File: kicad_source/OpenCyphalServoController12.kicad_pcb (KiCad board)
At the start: 2 copper layers, 81 x 57 mm, 90 parts, among them CN1 SM04B-SRSS-TB, CN10 GH_SM04B-GHS-TB, CN11 GH_SM04B-GHS-TB, CN12 Powerpole_2, CN13 DNI, CN14 DNI, CN2 CONN_02X03, CN3 CONN_02X03, CN4 CONN_02X03, CN5 CONN_02X03, CN6 CONN_02X03, CN7 CONN_02X03, CN8 SM04B-SRSS-TB, CN9 RASPBERRYPI_PICO, SW1 SPST, U1 24LC64, U2 MCP2515, U3 SN65HVD232, U4 RAA211650, Y1 16MHz

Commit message: started layout
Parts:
- moved L1 111.5 mm to (117.1, 68.4)
- moved L2 108.7 mm to (121.1, 80.4)
- moved L3 58.4 mm to (87.0, 92.0)
- moved C17 8.96 mm to (90.0, 73.1), turned to -90 degrees
- moved R18 8.06 mm to (94.0, 96.0)
- moved C3 8.00 mm to (94.0, 97.6)
- moved R17 8.00 mm to (94.0, 100.2)
- moved C12 5.54 mm to (92.4, 69.2), turned to 180 degrees
- moved R16 4.12 mm to (102.0, 96.0)
- moved R21 4.12 mm to (98.0, 96.0)
- moved C2 4.00 mm to (102.0, 97.6)
- moved C4 4.00 mm to (98.0, 97.6)
- moved R15 4.00 mm to (102.0, 100.2)
- moved R20 4.00 mm to (98.0, 100.2)
- moved R11 2.00 mm to (110.0, 62.0)
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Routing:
- net GND: track 0.00 -> 200.6 mm, vias 0 -> 23
- net VCC: track 0.00 -> 200.5 mm, vias 0 -> 4
- net +3V3: track 0.23 -> 162.8 mm, vias 0 -> 6
- net +BATT: track 0.00 -> 90.4 mm, vias 0 -> 4
- net +5V: track 0.00 -> 72.0 mm, vias 0 -> 2
- net /SERVO11: track 0.00 -> 66.8 mm, vias 0 -> 2
- net CANVCC: track 0.00 -> 63.3 mm, vias 0 -> 2
- net /SERVO10: track 0.00 -> 62.2 mm, vias 0 -> 2
- net /SERVO09: track 0.00 -> 42.2 mm, vias 0 -> 2
- net /MEAS_BATT: track 0.00 -> 38.8 mm
- net /SERVO08: track 0.00 -> 37.9 mm, vias 0 -> 2
- net /MEAS_CANVCC: track 0.00 -> 36.3 mm
- net /MEAS_5V: track 0.00 -> 35.8 mm
- net /I2C_SDA: track 0.00 -> 35.5 mm, vias 0 -> 2
- net /SERVO07: track 0.00 -> 34.8 mm, vias 0 -> 2
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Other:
- board text added: "<- USB this direction"
- board text added: "OpenCyphalServoController12 0.1"
- board text added: "find data and documentation at https://github.com/generationmake/OpenCyphalServoController12"
- board text removed: "NEOPIXEL"
- board text removed: "OpenCyphalPicoBase 0.2"
- board text removed: "RESERVED0"
- board text removed: "USB -> this direction"
- board text removed: "find data and documentation at https://github.com/generationmake/OpenCyphalPicoBase"
- board text removed: "servo"

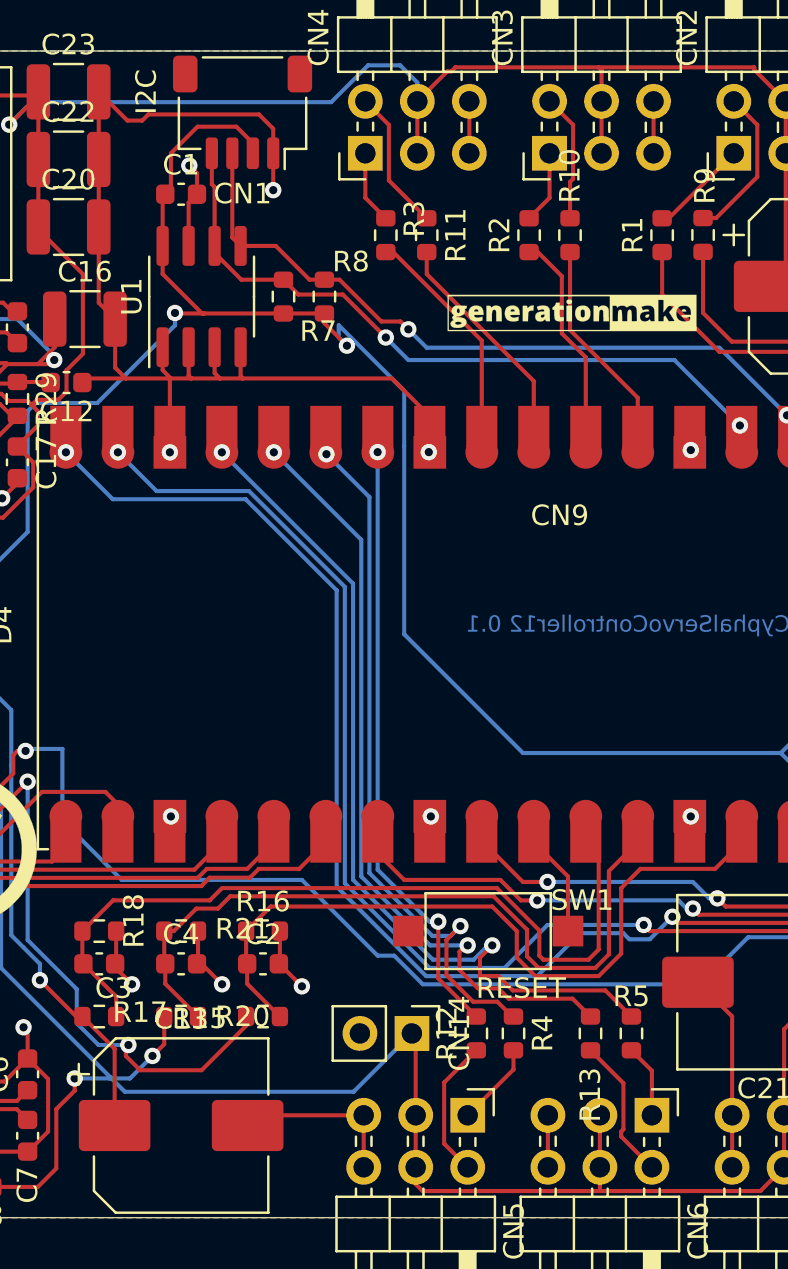
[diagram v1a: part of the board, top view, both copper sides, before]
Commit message: added additional capacitors on VCC
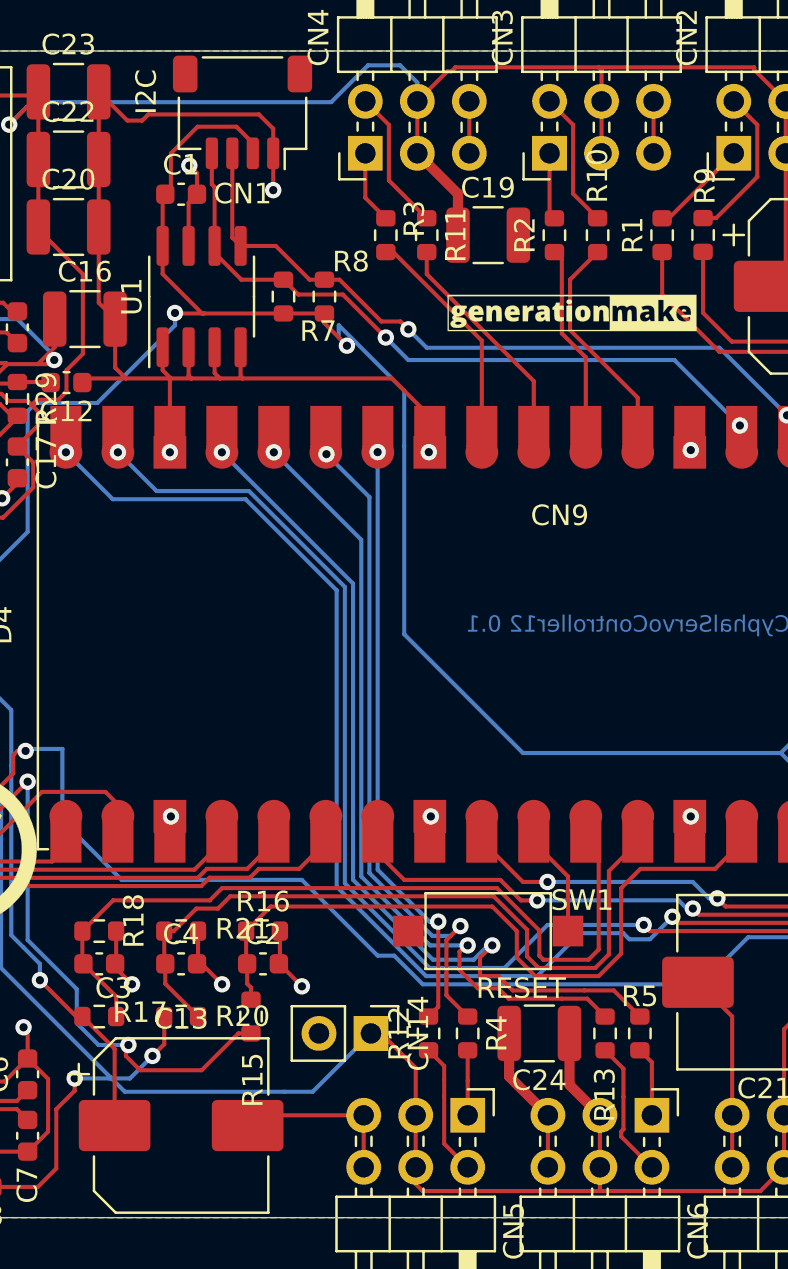
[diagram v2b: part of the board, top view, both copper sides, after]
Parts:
- added C19: 47uF 10V, Capacitor_SMD:C_1210_3225Metric, F.Cu at (113.0, 62.0)
- added C24: 47uF 10V, Capacitor_SMD:C_1210_3225Metric, F.Cu at (115.5, 101.0)
- R16, R21: value 10k -> 100k
- R17: value 100k -> 190k
- moved R12 2.33 mm to (110.1, 101.0)
- moved R4 2.24 mm to (112.0, 101.0)
- moved CN14 2.00 mm to (107.3, 101.0)
- moved R10 1.35 mm to (118.3, 62.0)
- moved R2 1.24 mm to (116.2, 62.0)
- moved R13 0.71 mm to (118.7, 101.0)
- moved R15 0.59 mm to (101.4, 100.2), turned to 90 degrees
- moved R5 0.41 mm to (120.4, 101.0)
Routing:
- net VCC: track 200.5 -> 208.5 mm
- net GND: track 200.6 -> 205.4 mm
- net /SERVO07: track 34.8 -> 33.2 mm
- net /MEAS_CANVCC: track 36.3 -> 34.9 mm
- net /SERVO07_R: track 4.10 -> 3.17 mm
- net /SERVO03: track 9.91 -> 9.15 mm
- net /SERVO08: track 37.9 -> 38.6 mm
- net /SERVO06: track 29.8 -> 29.2 mm
- net /SERVO02: track 9.89 -> 10.4 mm

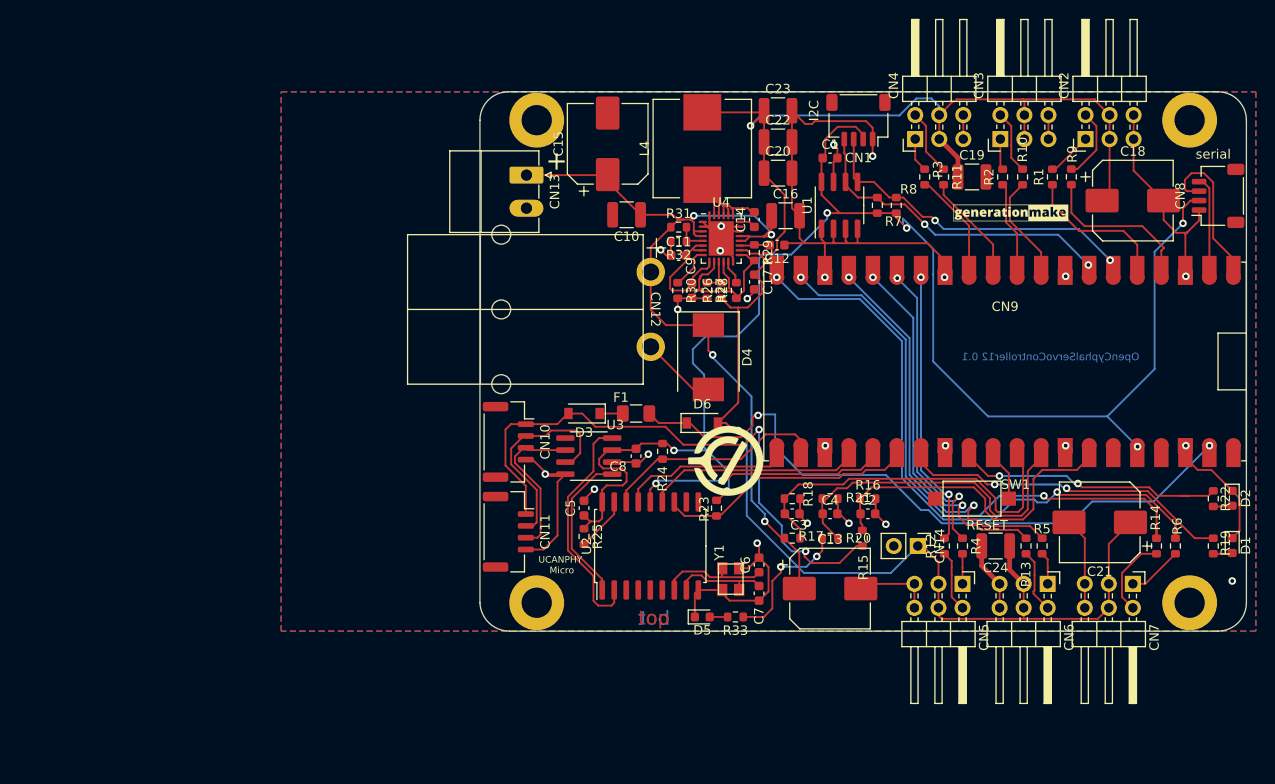
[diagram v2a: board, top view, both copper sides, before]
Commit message: added enable and power good for voltage regulator
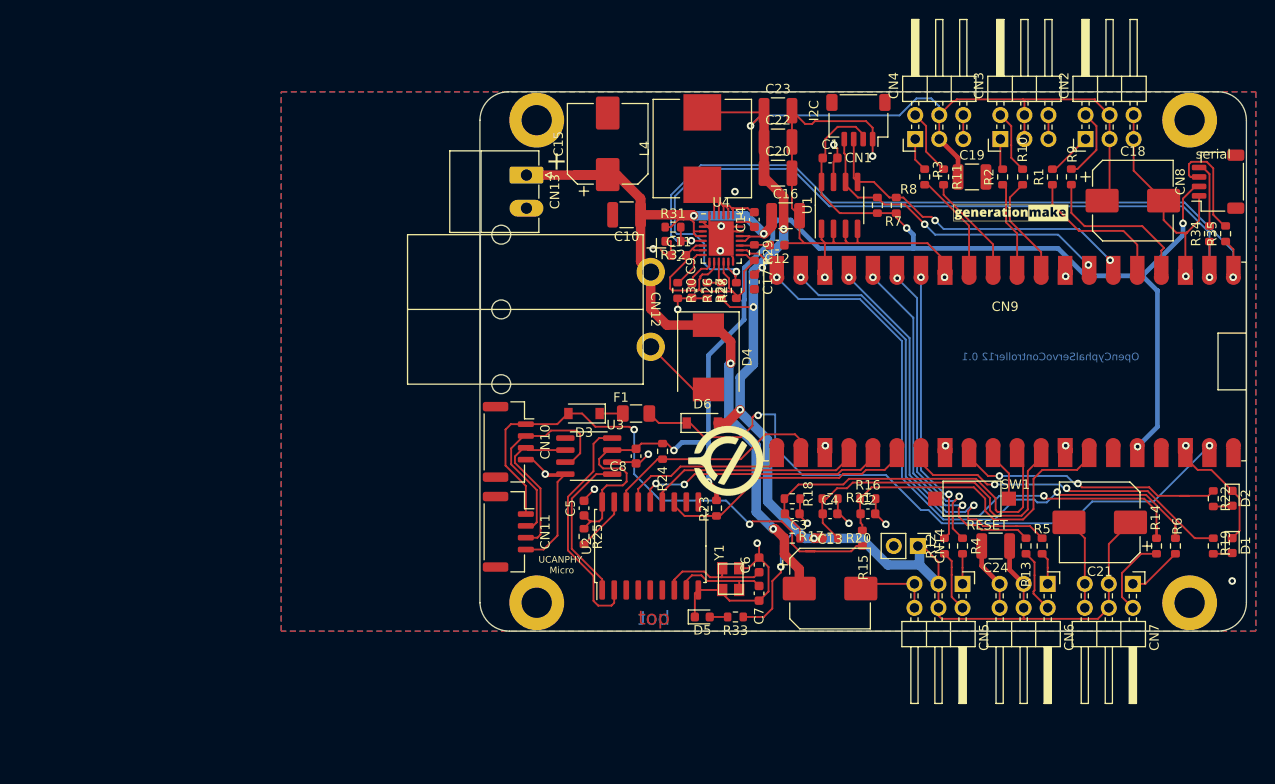
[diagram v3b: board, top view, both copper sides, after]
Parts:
- added R34: 100R, Resistor_SMD:R_0603_1608Metric, F.Cu at (138.1, 68.0)
- added R35: 100R, Resistor_SMD:R_0603_1608Metric, F.Cu at (139.8, 68.0)
- moved CN8 1.50 mm to (139.0, 62.5)
- moved R31 0.60 mm to (81.4, 67.3)
- moved R32 0.60 mm to (81.4, 68.8)
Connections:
- CN9 pad 1: /SER_TX -> VCC_EN
- CN9 pad 2: /SER_RX -> VCC_PG
- R28 pad 2: /Power/PG -> VCC_PG
- R31 pad 2: /Power/EN -> VCC_EN
- R32 pad 1: /Power/EN -> VCC_EN
- U4 pad 13: /Power/PG -> VCC_PG
- U4 pad 5: /Power/EN -> VCC_EN
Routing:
- net VCC_PG: track 0.00 -> 84.3 mm, vias 0 -> 2
- net VCC_EN: track 0.00 -> 80.6 mm, vias 0 -> 2
- net +BATT: track 90.4 -> 96.9 mm
- net +3V3: track 162.8 -> 157.5 mm, vias 6 -> 5
- net /SER_TX: track 15.9 -> 12.0 mm
- net VCC: track 208.5 -> 212.3 mm, vias 4 -> 7
- net CANVCC: track 62.9 -> 59.2 mm
- net /Power/EN: track 3.25 -> 0.00 mm
- net /SER_RX: track 9.53 -> 6.87 mm
- net /Power/PG: track 2.54 -> 0.00 mm
- net GND: track 205.4 -> 206.2 mm

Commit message: added mounting pads, beautified layout, run DRC
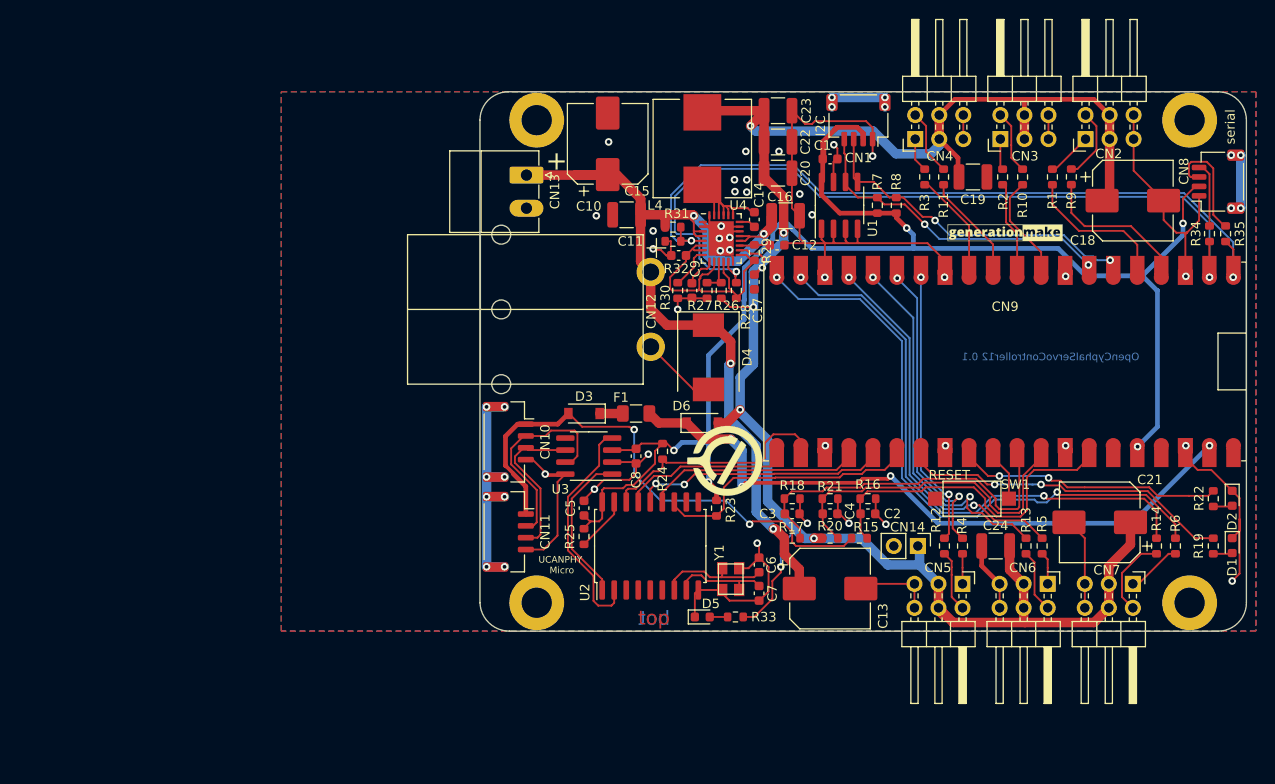
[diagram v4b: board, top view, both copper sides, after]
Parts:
- moved L1 2.18 mm to (116.5, 70.5)
- moved R15 0.31 mm to (101.1, 100.2), turned to 0 degrees
- moved C1 0.10 mm to (98.0, 60.1)
- moved C19 0.10 mm to (113.1, 62.0)
- moved L3 0.10 mm to (86.9, 92.0)
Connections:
- CN1 pad MP: (no net) -> /MP1
- CN10 pad MP: (no net) -> /MCP2515/MP3
- CN11 pad MP: (no net) -> /MCP2515/MP3
- CN8 pad MP: (no net) -> /MP2
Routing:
- net VCC: track 212.3 -> 247.0 mm
- net /MCP2515/MP3: track 0.00 -> 24.5 mm, vias 0 -> 8
- net GND: track 206.2 -> 220.0 mm, vias 23 -> 36
- net /MP2: track 0.00 -> 7.60 mm, vias 0 -> 4
- net /MP1: track 0.00 -> 7.60 mm, vias 0 -> 4
- net +BATT: track 96.9 -> 100.4 mm
- net +3V3: track 157.5 -> 160.4 mm
- net CANVCC: track 59.2 -> 56.5 mm
- net /SERVO09: track 42.6 -> 40.7 mm
- net MCP2515_CS: track 24.2 -> 26.0 mm
- net /SERVO11: track 66.8 -> 65.3 mm
- net /SERVO10: track 62.2 -> 60.7 mm
- net +5V: track 72.0 -> 70.6 mm, vias 2 -> 4
- net MCP2515_INT: track 26.9 -> 28.2 mm
- net /MEAS_BATT: track 38.8 -> 37.7 mm
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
